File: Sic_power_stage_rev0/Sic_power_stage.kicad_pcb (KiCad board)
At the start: 4 copper layers, 242.5 x 94.5 mm, 153 parts, among them J1 20021321-00006C4LF, J2 20021321-00006C4LF, J3 20021321-00006C4LF, J4 20021321-00006C4LF, J5 20021321-00006C4LF, J6 20021321-00006C4LF, J7 20021321-00006C4LF, J8 20021321-00006C4LF, Q1 NTBG014N120M3P, Q10 NTBG014N120M3P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

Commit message: SiC: modify routing in leg A - Change footprint for Amphenol connector
Signed-off-by: Ayarde Christian <cayarde@paltatech.com>
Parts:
- J1, J2, J3, J4, J5, J6, J7, J8: footprint conn-fci:CONN-20021321-00006C4LF -> conn-fci:CONN-20021321-00006C4LF-no-hole
- moved R24 103.1 mm to (92.5, 25.2)
- moved D8 67.8 mm to (20.8, 14.5), turned to -90 degrees
- moved STANDOFF10 65.2 mm to (-154.5, -81.5)
- moved STANDOFF3 65.2 mm to (-169.2, -81.5)
- moved STANDOFF6 65.2 mm to (-183.8, -81.2)
- moved STANDOFF7 65.2 mm to (-128.5, -81.7)
- moved STANDOFF9 65.2 mm to (-140.5, -81.7)
- moved R14 63.2 mm to (4.50, -5.50), turned to 90 degrees
- moved D7 30.5 mm to (-31.5, 0.00), turned to -90 degrees
- moved D4 8.28 mm to (-52.2, 14.5)
- moved R6 6.10 mm to (-58.2, 15.2), turned to 180 degrees
- moved C40 5.55 mm to (-27.0, 20.2), turned to 180 degrees
- moved C2 5.00 mm to (-58.2, 17.0), turned to 180 degrees
- moved D2 4.32 mm to (-58.2, 19.2), turned to 180 degrees
- moved R34 4.30 mm to (-36.0, 8.80)
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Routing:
- net /Half Bridge A/S_BOT: track 87.1 -> 136.6 mm
- net /Half Bridge A/G_BOT: track 65.6 -> 111.5 mm, vias 4 -> 3
- net /Half Bridge B/NTC_BOT: track 0.00 -> 36.7 mm, vias 0 -> 2
- net /Half Bridge A/G_TOP: track 77.1 -> 106.3 mm
- net /Half Bridge B/D_TOP: track 0.00 -> 29.1 mm, vias 1 -> 0
- net /Half Bridge B/SHUNT+: track 0.00 -> 27.0 mm
- net /Half Bridge B/SHUNT-: track 0.00 -> 27.0 mm
- net /Half Bridge A/S_TOP: track 100.9 -> 122.4 mm
- net /Half Bridge A/D_TOP: track 0.00 -> 19.5 mm
- net /VBUS_M: track 5.79 -> 22.1 mm
- net /Half Bridge B/G_BOT: track 62.3 -> 76.8 mm
- net VBUS: track 62.9 -> 75.3 mm, vias 1345 -> 1303
- net PWRGND: track 11.8 -> 22.0 mm, vias 371 -> 458
- net /Half Bridge B/S_BOT: track 84.3 -> 94.4 mm
- net /Half Bridge B/G_TOP: track 64.1 -> 73.1 mm
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- added copper zone on B.Cu, net /Half Bridge A/PHASE

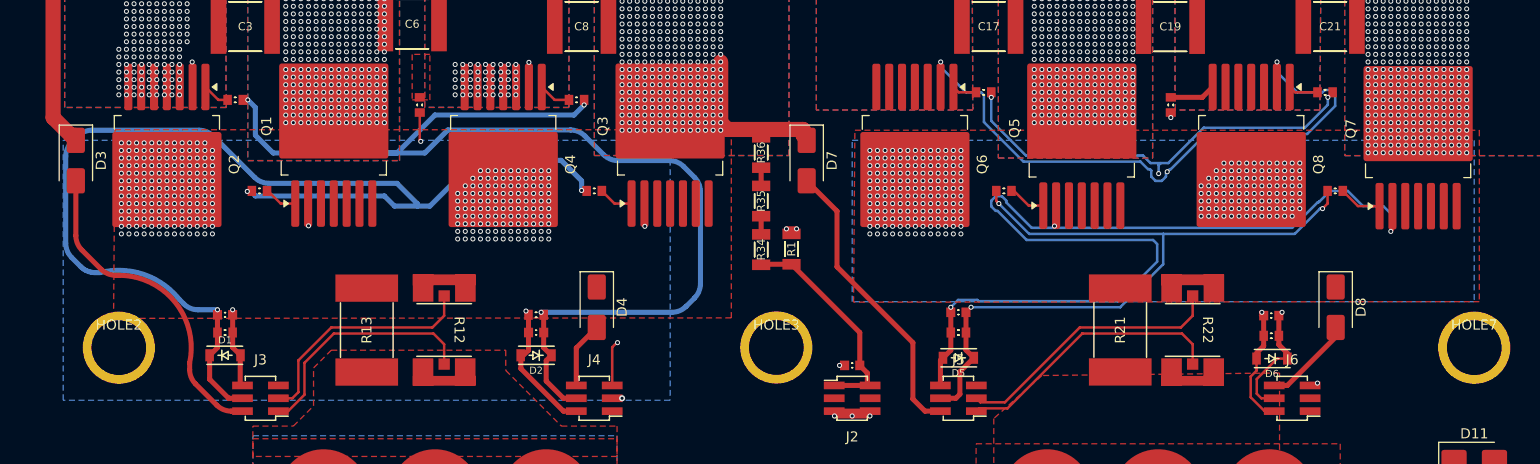
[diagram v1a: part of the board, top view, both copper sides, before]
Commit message: SiC: finish routing on leg B
Signed-off-by: Ayarde Christian <cayarde@paltatech.com>
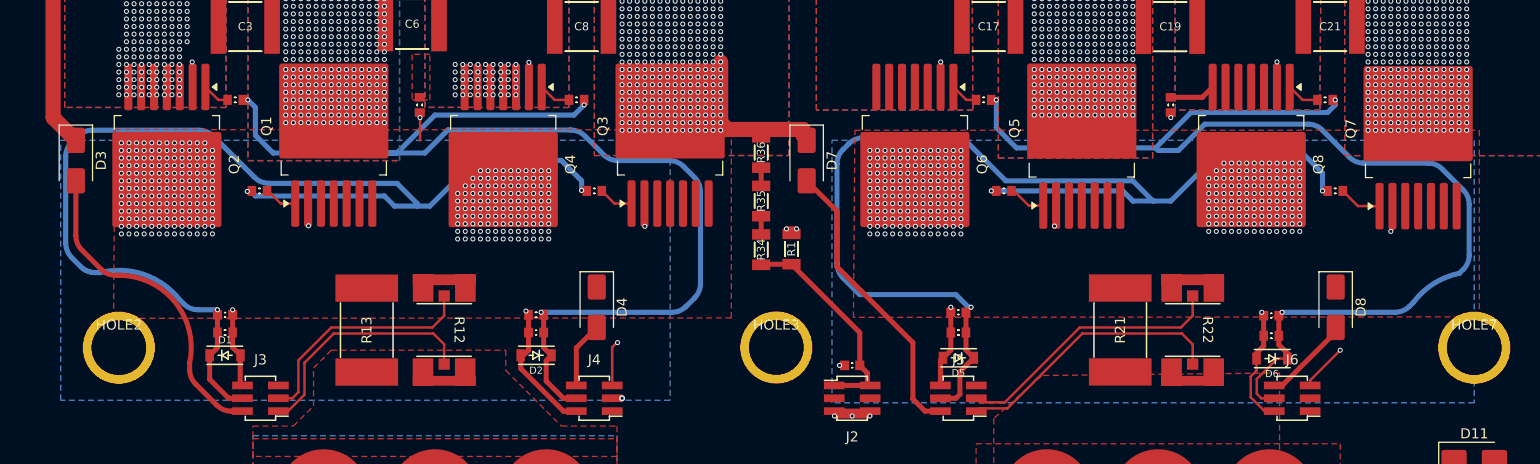
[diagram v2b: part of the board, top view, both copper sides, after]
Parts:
- moved R19 0.75 mm to (-14.0, -6.00)
- moved R20 0.75 mm to (19.8, -6.00)
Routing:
- net /Half Bridge B/G_TOP: track 73.1 -> 110.8 mm
- net /Half Bridge B/S_BOT: track 94.4 -> 129.6 mm, vias 4 -> 3
- net /Half Bridge B/G_BOT: track 76.8 -> 107.2 mm, vias 4 -> 3
- net /Half Bridge B/S_TOP: track 100.2 -> 123.9 mm
- net /Half Bridge B/NTC_BOT: track 36.7 -> 41.9 mm
- net /Half Bridge A/NTC_BOT: track 43.0 -> 44.7 mm
- net VBUS: vias 1303 -> 1247
- net /Half Bridge B/node_a: vias 261 -> 283
- added copper zone on In1.Cu, net /Half Bridge A/node_a
- added copper zone on In1.Cu, net /Half Bridge B/node_a

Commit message: SiC: define routing for leg C
Signed-off-by: Ayarde Christian <cayarde@paltatech.com>
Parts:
- moved C27 226.4 mm to (49.0, 15.2)
- moved D9 190.2 mm to (49.0, 19.2)
- moved R41 123.0 mm to (-177.5, 11.8), turned to 90 degrees
- moved R40 115.9 mm to (-177.5, 17.2), turned to -90 degrees
- moved R30 113.9 mm to (94.0, -6.00), turned to 180 degrees
- moved R42 109.6 mm to (-177.5, 22.2), turned to -90 degrees
- moved D10 57.3 mm to (99.8, 30.8), turned to 180 degrees
- moved R29 55.9 mm to (60.5, -6.00), turned to 180 degrees
- moved R28 53.1 mm to (95.2, 3.00), turned to 0 degrees
- moved R25 42.8 mm to (49.0, 17.0), turned to 0 degrees
- moved R26 42.1 mm to (89.2, 17.2), turned to 180 degrees
- moved R24 33.7 mm to (78.8, -5.50), turned to 90 degrees
- moved R27 31.4 mm to (62.2, 3.00), turned to 0 degrees
- moved D11 30.5 mm to (42.2, 0.00), turned to -90 degrees
- moved R23 22.7 mm to (1.75, 66.2)
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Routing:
- net /Half Bridge C/G_TOP: track 0.00 -> 99.1 mm, vias 0 -> 2
- net /Half Bridge C/S_TOP: track 0.00 -> 12.0 mm, vias 0 -> 2
- net /Half Bridge C/node_a: track 0.00 -> 6.07 mm, vias 0 -> 247
- net /Half Bridge C/GT2: track 0.00 -> 4.48 mm
- net /Half Bridge C/GT1: track 0.00 -> 3.71 mm
- net VBUS: vias 1247 -> 1863
- added copper zone on B.Cu, net /Half Bridge C/node_a

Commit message: Sic: change layer for gate and driver source
Signed-off-by: Ayarde Christian <cayarde@paltatech.com>
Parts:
- moved HOLE6 471.4 mm to (-298.2, -84.5)
- moved R31 468.9 mm to (-372.4, -54.2), turned to 0 degrees
- moved C39 426.6 mm to (-310.0, 23.0)
- moved C13 400.4 mm to (-323.0, 23.0)
- moved C26 400.4 mm to (-335.5, 23.0)
- moved R23 386.5 mm to (-371.4, -34.8)
- moved R3 381.1 mm to (-377.9, 9.50)
- moved R11 324.8 mm to (-371.2, -45.2)
- moved C28 162.0 mm to (-283.4, -6.82)
- moved C41 162.0 mm to (-319.6, -20.0)
- moved D13 162.0 mm to (-322.1, -23.5)
- moved DS1 162.0 mm to (-323.9, -19.9)
- moved HOLE1 162.0 mm to (-427.1, -71.8)
- moved HOLE4 162.0 mm to (-298.0, -49.0)
- moved HOLE5 162.0 mm to (-298.2, -59.2)
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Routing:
- net /Half Bridge C/S_TOP: track 12.0 -> 115.6 mm
- net /Half Bridge B/NTC_BOT: track 41.9 -> 52.9 mm
- net /Half Bridge A/NTC_BOT: track 44.7 -> 52.9 mm
- net /Half Bridge C/G_TOP: track 99.1 -> 100.4 mm, vias 2 -> 3
- added copper zone on In2.Cu, net /Half Bridge C/node_a

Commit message: Sic: finish leg C
Signed-off-by: Ayarde Christian <christianayarde@gmail.com>
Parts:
- moved C28 369.8 mm to (85.8, 15.2), turned to 180 degrees
- moved D12 51.4 mm to (109.5, 14.5), turned to -90 degrees
- moved D10 18.3 mm to (85.5, 19.2)
- moved R26 3.50 mm to (85.8, 17.2)
- moved R32 0.50 mm to (76.2, 16.8)
- moved R33 0.50 mm to (68.5, 16.8)
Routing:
- net /Half Bridge C/S_BOT: track 0.00 -> 143.1 mm, vias 0 -> 3
- net /Half Bridge C/G_BOT: track 0.00 -> 119.9 mm, vias 0 -> 3
- net /Half Bridge C/NTC_BOT: track 0.00 -> 55.9 mm, vias 0 -> 2
- net /Half Bridge A/NTC_BOT: track 52.9 -> 51.3 mm
- net /Half Bridge C/S_TOP: track 115.6 -> 116.5 mm
- net VBUS: vias 1863 -> 1849
- added copper zone on In1.Cu, net /Half Bridge C/node_a

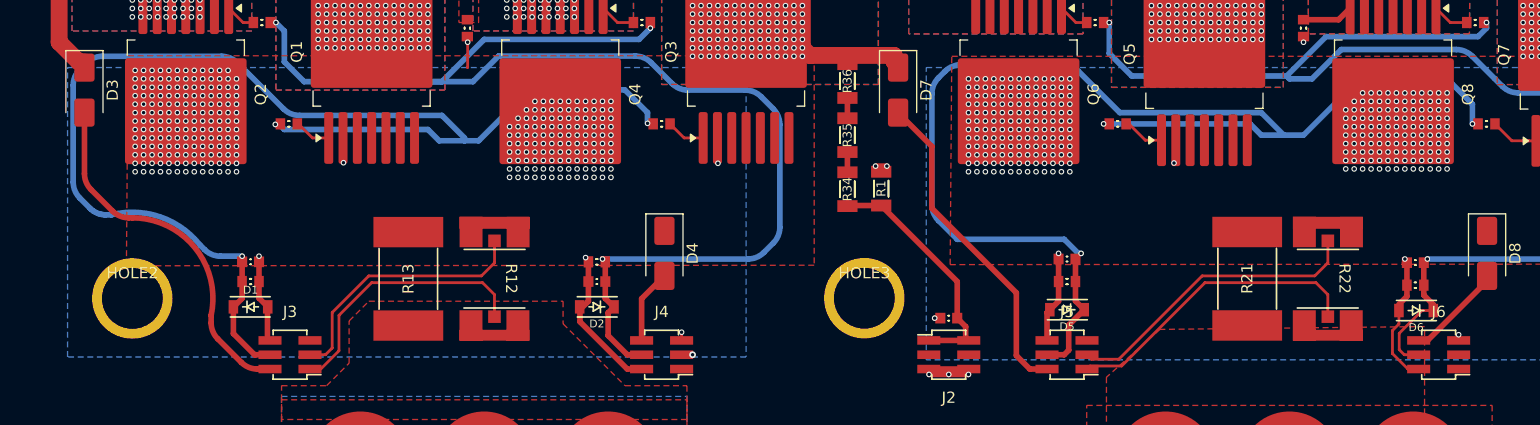
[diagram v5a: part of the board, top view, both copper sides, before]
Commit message: Sic: Change track shape for NTC leg C
Signed-off-by: Ayarde Christian <christianayarde@gmail.com>
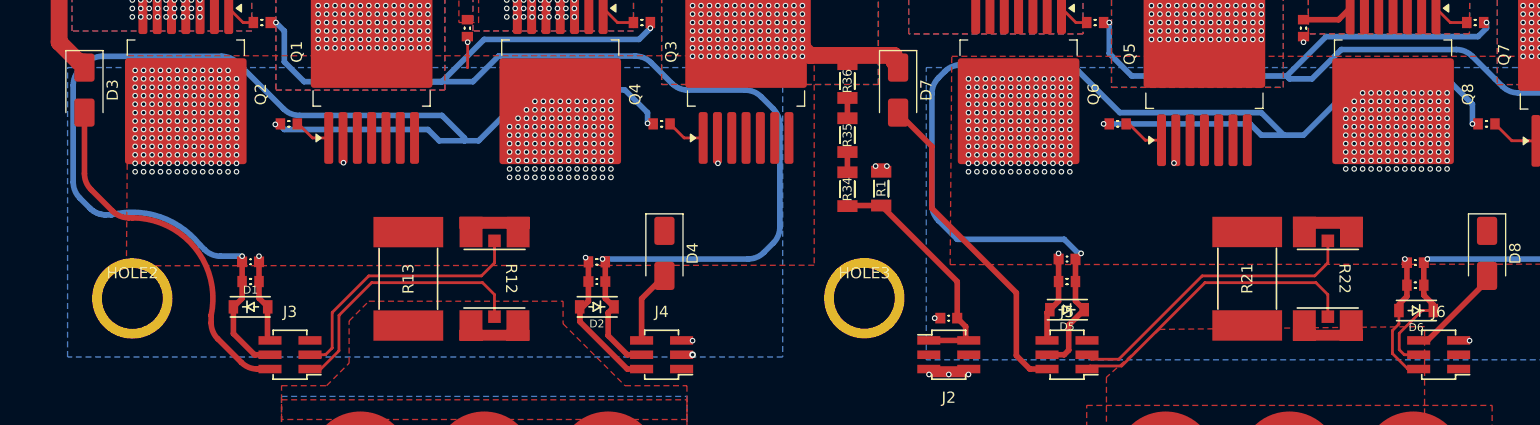
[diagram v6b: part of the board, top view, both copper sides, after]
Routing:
- net /Half Bridge C/NTC_BOT: track 55.9 -> 44.2 mm
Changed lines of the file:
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@@
 	)
 	(gr_arc
+		(start 92.5 18.25)
+		(mid 95.019775 13.115756)
+		(end 100.526495 11.571161)
+		(stroke
+			(width 0.25)
+			(type solid)
+		)
+		(layer "In1.Cu")
+		(net 25)
+	)
+	(gr_arc
 		(start 28.483357 13.987518)
 		(mid 30.26442 12.285312)
@@
 	)
 	(segment
-		(start -50.725 21.5)
-		(end -50.725 22.23)
+		(start -49.75 22.25)
+		(end -49.77 22.23)
 		(width 0.25)
 		(layer "F.Cu")
@@
 	)
 	(segment
+		(start -49.77 22.23)
+		(end -50.725 22.23)
+		(width 0.25)
+		(layer "F.Cu")
+		(net 14)
+	)
+	(segment
 		(start -69.722503 -2.025417)
 		(end -69.722503 -4.25)
@@
 	)
 	(via
-		(at -50.725 21.5)
+		(at -49.75 22.25)
 		(size 0.5)
 		(drill 0.3)
@@
 	)
 	(segment
-		(start -51.626 -1.876)
-		(end -67.348503 -1.876)
-		(width 0.25)
-		(layer "In1.Cu")
-		(net 14)
-	)
-	(segment
-		(start -50.725 21.5)
-		(end -50.113128 21.5)
-		(width 0.25)
-		(layer "In1.Cu")
-		(net 14)
-	)
-	(segment
-		(start -67.348503 -1.876)
-		(end -69.722503 -4.25)
+		(start -49.75 22.25)
+		(end -49.75 21.5)
 		(width 0.25)
 		(layer "In1.Cu")
@@
 	)
 	(segment
-		(start -44.624 16.124)
-		(end -44.624 5.126)
+		(start -44.624 5.126)
+		(end -51.626 -1.876)
 		(width 0.25)
 		(layer "In1.Cu")
@@
 	)
 	(segment
-		(start -46.636872 18.136872)
-		(end -44.624 16.124)
+		(start -51.626 -1.876)
+		(end -67.348503 -1.876)
 		(width 0.25)
 		(layer "In1.Cu")
@@
 	)
 	(segment
-		(start -44.624 5.126)
-		(end -51.626 -1.876)
+		(start -67.348503 -1.876)
+		(end -69.722503 -4.25)
 		(width 0.25)
 		(layer "In1.Cu")
@@
 	)
 	(segment
-		(start -50.113128 21.5)
-		(end -46.75 18.136872)
+		(start -49.75 21.5)
+		(end -44.624 16.374)
 		(width 0.25)
 		(layer "In1.Cu")
@@
 	)
 	(segment
-		(start -46.75 18.136872)
-		(end -46.636872 18.136872)
+		(start -44.624 16.374)
+		(end -44.624 5.126)
 		(width 0.25)
 		(layer "In1.Cu")
@@
 	)
 	(segment
+		(start 19.23 22.23)
+		(end 18.275 22.23)
+		(width 0.25)
+		(layer "F.Cu")
+		(net 19)
+	)
+	(segment
 		(start 4.5 -4.75)
 		(end 4.5 -4.5)
@@
 	)
 	(segment
-		(start 18.275 21.725)
-		(end 18.275 22.23)
+		(start 19.25 22.25)
+		(end 19.23 22.23)
 		(width 0.25)
 		(layer "F.Cu")
@@
 	)
 	(via
-		(at 18.275 21.725)
+		(at 19.25 22.25)
 		(size 0.5)
 		(drill 0.3)
@@
 	)
 	(segment
-		(start 21.25 -2.75)
-		(end 6 -2.75)
+		(start 6 -2.75)
+		(end 4.5 -4.25)
 		(width 0.25)
 		(layer "In1.Cu")
@@
 	)
 	(segment
-		(start 18.275 21.725)
-		(end 21.775 21.725)
+		(start 19.25 22.25)
+		(end 21.25 22.25)
 		(width 0.25)
 		(layer "In1.Cu")
@@
 	)
 	(segment
-		(start 21.775 21.725)
+		(start 21.25 22.25)
 		(end 29.75 13.75)
 		(width 0.25)
@@
 	)
 	(segment
-		(start 6 -2.75)
-		(end 4.5 -4.25)
+		(start 29.75 13.75)
+		(end 29.75 5.75)
 		(width 0.25)
 		(layer "In1.Cu")
@@
 	)
 	(segment
-		(start 29.75 5.75)
-		(end 21.25 -2.75)
+		(start 21.25 -2.75)
+		(end 6 -2.75)
 		(width 0.25)
 		(layer "In1.Cu")
@@
 	)
 	(segment
-		(start 29.75 13.75)
-		(end 29.75 5.75)
+		(start 29.75 5.75)
+		(end 21.25 -2.75)
 		(width 0.25)
 		(layer "In1.Cu")
@@
 	)
 	(segment
-		(start 95.567279 -2.75)
-		(end 104 5.682721)
+		(start 80.5 -2.75)
+		(end 78.75 -4.5)
 		(width 0.25)
 		(layer "In1.Cu")
@@
 	)
 	(segment
-		(start 78.75 -4.5)
+		(start 95.567279 -2.75)
 		(end 80.5 -2.75)
 		(width 0.25)
@@
 	)
 	(segment
-		(start 97.030425 11.5)
-		(end 88.25 20.280425)
+		(start 104 5.682721)
+		(end 95.567279 -2.75)
 		(width 0.25)
 		(layer "In1.Cu")
@@
 	)
 	(segment
-		(start 104 5.682721)
+		(start 104 9.75)
+		(end 104 5.682721)
+		(width 0.25)
+		(layer "In1.Cu")
+		(net 25)
+	)
+	(segment
+		(start 103.057519 10.692481)
 		(end 104 9.75)
 		(width 0.25)
@@
 	)
 	(segment
-		(start 104 9.75)
-		(end 102.25 11.5)
+		(start 92.5 18.25)
+		(end 92.5 18.257359)
 		(width 0.25)
 		(layer "In1.Cu")
@@
 	)
 	(segment
-		(start 80.5 -2.75)
-		(end 95.567279 -2.75)
+		(start 88.507359 22.25)
+		(end 88.25 22.25)
 		(width 0.25)
 		(layer "In1.Cu")
@@
 	)
 	(segment
-		(start 102.25 11.5)
-		(end 97.030425 11.5)
+		(start 100.526495 11.571161)
+		(end 100.936198 11.571161)
 		(width 0.25)
 		(layer "In1.Cu")
@@
 	)
 	(segment
-		(start 88.25 20.280425)
-		(end 88.25 22.25)
+		(start 91.62132 20.37868)
+		(end 90.628679 21.371321)
+		(width 0.25)
+		(layer "In1.Cu")
+		(net 25)
+	)
+	(arc
+		(start 90.628679 21.371321)
+		(mid 89.655409 22.021639)
+		(end 88.507359 22.25)
+		(width 0.25)
+		(layer "In1.Cu")
+		(net 25)
+	)
+	(arc
+		(start 92.5 18.257359)
+		(mid 92.271638 19.40541)
+		(end 91.62132 20.37868)
+		(width 0.25)
+		(layer "In1.Cu")
+		(net 25)
+	)
+	(arc
+		(start 100.936198 11.571161)
+		(mid 102.084249 11.342799)
+		(end 103.057519 10.692481)
 		(width 0.25)
 		(layer "In1.Cu")
@@
 		(polygon
 			(pts
-				(xy -105.25 -2) (xy -45 -2) (xy -45 23.7) (xy -105.25 23.7)
+				(xy -105.25 -2) (xy -41.75 -2) (xy -41.75 23.7) (xy -105.25 23.7)
 			)
 		)
